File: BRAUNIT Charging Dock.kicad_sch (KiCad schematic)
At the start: 0 parts

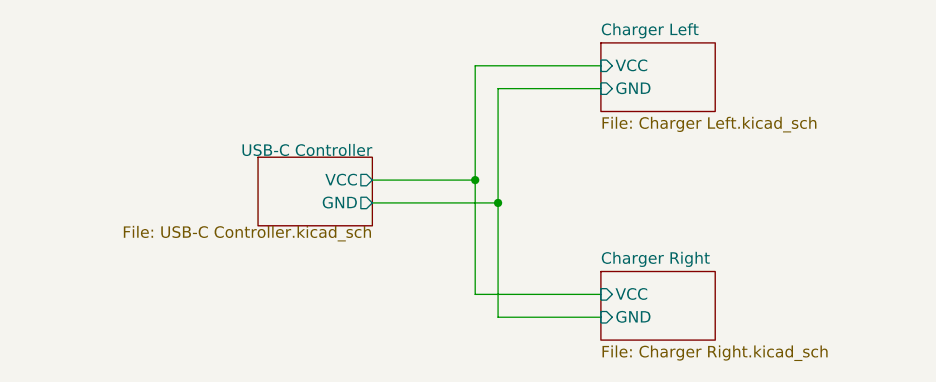
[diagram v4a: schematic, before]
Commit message: Specify LED, resistors, and start on USB-C circuit
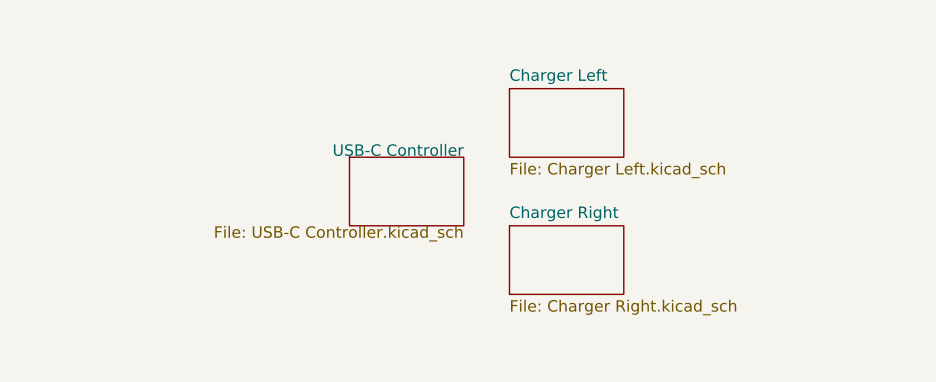
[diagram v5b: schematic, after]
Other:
- sheet Charger Left ports: added none; removed GND, VCC
- sheet Charger Right ports: added none; removed GND, VCC
- sheet USB-C Controller ports: added none; removed GND, VCC
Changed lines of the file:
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@@
 (kicad_sch (version 20211123) (generator eeschema)
   (paper "A4")
-  (junction (at 153.67 93.98) (diameter 0) (color 0 0 0 0)
-  )
-  (junction (at 151.13 91.44) (diameter 0) (color 0 0 0 0)
-  )
-  (wire (pts (xy 165.1 78.74) (xy 151.13 78.74))
-    (stroke (width 0) (type default) (color 0 0 0 0))
-  )
-  (wire (pts (xy 151.13 78.74) (xy 151.13 91.44))
-    (stroke (width 0) (type default) (color 0 0 0 0))
-  )
-  (wire (pts (xy 165.1 106.68) (xy 153.67 106.68))
-    (stroke (width 0) (type default) (color 0 0 0 0))
-  )
-  (wire (pts (xy 139.7 93.98) (xy 153.67 93.98))
-    (stroke (width 0) (type default) (color 0 0 0 0))
-  )
-  (wire (pts (xy 153.67 93.98) (xy 153.67 81.28))
-    (stroke (width 0) (type default) (color 0 0 0 0))
-  )
-  (wire (pts (xy 165.1 104.14) (xy 151.13 104.14))
-    (stroke (width 0) (type default) (color 0 0 0 0))
-  )
-  (wire (pts (xy 153.67 81.28) (xy 165.1 81.28))
-    (stroke (width 0) (type default) (color 0 0 0 0))
-  )
-  (wire (pts (xy 151.13 104.14) (xy 151.13 91.44))
-    (stroke (width 0) (type default) (color 0 0 0 0))
-  )
-  (wire (pts (xy 153.67 106.68) (xy 153.67 93.98))
-    (stroke (width 0) (type default) (color 0 0 0 0))
-  )
-  (wire (pts (xy 139.7 91.44) (xy 151.13 91.44))
-    (stroke (width 0) (type default) (color 0 0 0 0))
-  )
-  (sheet (at 165.1 101.6) (size 12.7 7.62) (fields_autoplaced)
+  (sheet (at 154.94 96.52) (size 12.7 7.62) (fields_autoplaced)
     (stroke (width 0.1524) (type solid) (color 0 0 0 0))
     (fill (color 0 0 0 0.0000))
-    (property "Sheet name" "Charger Right" (id 0) (at 165.1 100.8884 0)
+    (property "Sheet name" "Charger Right" (id 0) (at 154.94 95.8084 0)
       (effects (font (size 1.27 1.27)) (justify left bottom))
     )
-    (property "Sheet file" "Charger Right.kicad_sch" (id 1) (at 165.1 109.8046 0)
+    (property "Sheet file" "Charger Right.kicad_sch" (id 1) (at 154.94 104.7246 0)
       (effects (font (size 1.27 1.27)) (justify left top))
     )
-    (pin "VCC" input (at 165.1 104.14 180)
-      (effects (font (size 1.27 1.27)) (justify left))
-    )
-    (pin "GND" input (at 165.1 106.68 180)
-      (effects (font (size 1.27 1.27)) (justify left))
-    )
-  )
-  (sheet (at 127 88.9) (size 12.7 7.62)
+  )
+  (sheet (at 137.16 88.9) (size 12.7 7.62)
     (stroke (width 0.1524) (type solid) (color 0 0 0 0))
     (fill (color 0 0 0 0.0000))
-    (property "Sheet name" "USB-C Controller" (id 0) (at 139.7 88.9 0)
+    (property "Sheet name" "USB-C Controller" (id 0) (at 149.86 88.9 0)
       (effects (font (size 1.27 1.27)) (justify right bottom))
     )
-    (property "Sheet file" "USB-C Controller.kicad_sch" (id 1) (at 139.7 96.52 0)
+    (property "Sheet file" "USB-C Controller.kicad_sch" (id 1) (at 149.86 96.52 0)
       (effects (font (size 1.27 1.27)) (justify right top))
     )
-    (pin "VCC" output (at 139.7 91.44 0)
-      (effects (font (size 1.27 1.27)) (justify right))
-    )
-    (pin "GND" output (at 139.7 93.98 0)
-      (effects (font (size 1.27 1.27)) (justify right))
-    )
-  )
-  (sheet (at 165.1 76.2) (size 12.7 7.62) (fields_autoplaced)
+  )
+  (sheet (at 154.94 81.28) (size 12.7 7.62) (fields_autoplaced)
     (stroke (width 0.1524) (type solid) (color 0 0 0 0))
     (fill (color 0 0 0 0.0000))
-    (property "Sheet name" "Charger Left" (id 0) (at 165.1 75.4884 0)
+    (property "Sheet name" "Charger Left" (id 0) (at 154.94 80.5684 0)
       (effects (font (size 1.27 1.27)) (justify left bottom))
     )
-    (property "Sheet file" "Charger Left.kicad_sch" (id 1) (at 165.1 84.4046 0)
+    (property "Sheet file" "Charger Left.kicad_sch" (id 1) (at 154.94 89.4846 0)
       (effects (font (size 1.27 1.27)) (justify left top))
-    )
-    (pin "VCC" input (at 165.1 78.74 180)
-      (effects (font (size 1.27 1.27)) (justify left))
-    )
-    (pin "GND" input (at 165.1 81.28 180)
-      (effects (font (size 1.27 1.27)) (justify left))
     )
   )
@@
       (reference "#PWR0118") (unit 1) (value "VCC") (footprint "")
     )
+    (path "/9b64bdde-614f-48a8-af9a-410c135af729/c2b890dc-1bcb-4bb5-ba06-2c2912d9fa75"
+      (reference "#PWR0119") (unit 1) (value "GND") (footprint "")
+    )
+    (path "/9b64bdde-614f-48a8-af9a-410c135af729/24ae74de-90b1-4c74-b26c-2bc1b1d9631a"
+      (reference "#PWR0120") (unit 1) (value "GND") (footprint "")
+    )
+    (path "/9b64bdde-614f-48a8-af9a-410c135af729/973720a6-f461-4d46-b2fe-59915df69d25"
+      (reference "#PWR?") (unit 1) (value "GND") (footprint "")
+    )
+    (path "/9b64bdde-614f-48a8-af9a-410c135af729/fade7e8a-567f-48a0-80a0-084bb672c228"
+      (reference "#PWR?") (unit 1) (value "GND") (footprint "")
+    )
     (path "/b2909144-61aa-40b6-b4ee-631beaa2767a/9c4ca713-efc0-464c-a186-be30f9d06ebd"
       (reference "C1") (unit 1) (value "1uF") (footprint "Capacitor_SMD:C_0805_2012Metric")
@@
       (reference "J2") (unit 1) (value "BRAUNIT") (footprint "BRAUNIT Charger:Blade_1x04_P2.5mm_Vertical_BRAUNIT_Loose")
     )
+    (path "/9b64bdde-614f-48a8-af9a-410c135af729/7708a299-04e9-4626-b47c-faab41f3665c"
+      (reference "J3") (unit 1) (value "USB_C_Receptacle") (footprint "Connector_USB:USB_C_Receptacle_HRO_TYPE-C-31-M-12")
+    )
     (path "/b2909144-61aa-40b6-b4ee-631beaa2767a/c2edbe55-ed11-4e1b-b28d-2bb3bb3eda31"
       (reference "L1") (unit 1) (value "22uH") (footprint "Inductor_SMD:L_10.4x10.4_H4.8")
@@
     )
     (path "/b2909144-61aa-40b6-b4ee-631beaa2767a/16173b27-1c6b-42e2-8ac3-2bad8b6f5b16"
-      (reference "R1") (unit 1) (value "R") (footprint "")
+      (reference "R1") (unit 1) (value "2k7") (footprint "Resistor_SMD:R_0603_1608Metric")
     )
     (path "/b2909144-61aa-40b6-b4ee-631beaa2767a/0a6c358c-9a42-47bc-980c-079c2ff3565d"
-      (reference "R2") (unit 1) (value "R") (footprint "")
+      (reference "R2") (unit 1) (value "2k7") (footprint "Resistor_SMD:R_0603_1608Metric")
     )
     (path "/b2909144-61aa-40b6-b4ee-631beaa2767a/0418d433-93ed-42f8-98e2-be9abb9aa807"
@@
     )
     (path "/7a6d3a70-dd46-4bb3-a764-a6a3c3bbb5ac/d98162a8-6c95-45e2-b639-1663c189ccb4"
-      (reference "R5") (unit 1) (value "R") (footprint "")
+      (reference "R5") (unit 1) (value "2k7") (footprint "Resistor_SMD:R_0603_1608Metric")
     )
     (path "/7a6d3a70-dd46-4bb3-a764-a6a3c3bbb5ac/f9826834-5766-41aa-8b02-b92d17ac6c78"
-      (reference "R6") (unit 1) (value "R") (footprint "")
+      (reference "R6") (unit 1) (value "2k7") (footprint "Resistor_SMD:R_0603_1608Metric")
     )
     (path "/7a6d3a70-dd46-4bb3-a764-a6a3c3bbb5ac/a28c4a72-8926-48a4-96fc-f7a28adb6d1b"
@@
     )
     (path "/b2909144-61aa-40b6-b4ee-631beaa2767a/02297bbb-ab4c-4b32-b01f-a1a47b5f8881"
-      (reference "Rcs1") (unit 1) (value "0.1") (footprint "BRAUNIT Charger:R_Shunt_2010_5025Metric")
+      (reference "Rcs1") (unit 1) (value "0R1") (footprint "BRAUNIT Charger:R_Shunt_2010_5025Metric")
     )
     (path "/7a6d3a70-dd46-4bb3-a764-a6a3c3bbb5ac/ad8bebc5-2f22-4688-be1f-ab19304ec83b"
-      (reference "Rcs2") (unit 1) (value "0.1") (footprint "BRAUNIT Charger:R_Shunt_2010_5025Metric")
+      (reference "Rcs2") (unit 1) (value "0R1") (footprint "BRAUNIT Charger:R_Shunt_2010_5025Metric")
     )
     (path "/b2909144-61aa-40b6-b4ee-631beaa2767a/4f7d8c71-9c89-47e1-bdd9-71ea2ff9470f"
@@
       (reference "U2") (unit 1) (value "CN3702") (footprint "Package_SO:TSSOP-16_4.4x5mm_P0.65mm")
     )
-  )
+    (path "/9b64bdde-614f-48a8-af9a-410c135af729/602e1c35-c9ad-450d-a65b-6720b62fe2e6"
+      (reference "U3") (unit 1) (value "STUSB4500QTR") (footprint "Package_DFN_QFN:QFN-24-1EP_4x4mm_P0.5mm_EP2.7x2.7mm")
+    )
+  )
